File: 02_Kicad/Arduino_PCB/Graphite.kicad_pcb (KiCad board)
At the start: 2 copper layers, 68.6 x 53.3 mm, 21 parts, among them J1 Power, J2 Digital/PWM, J3 Analog, J4 Digital/PWM, U1 LTC1050, U2 HC05

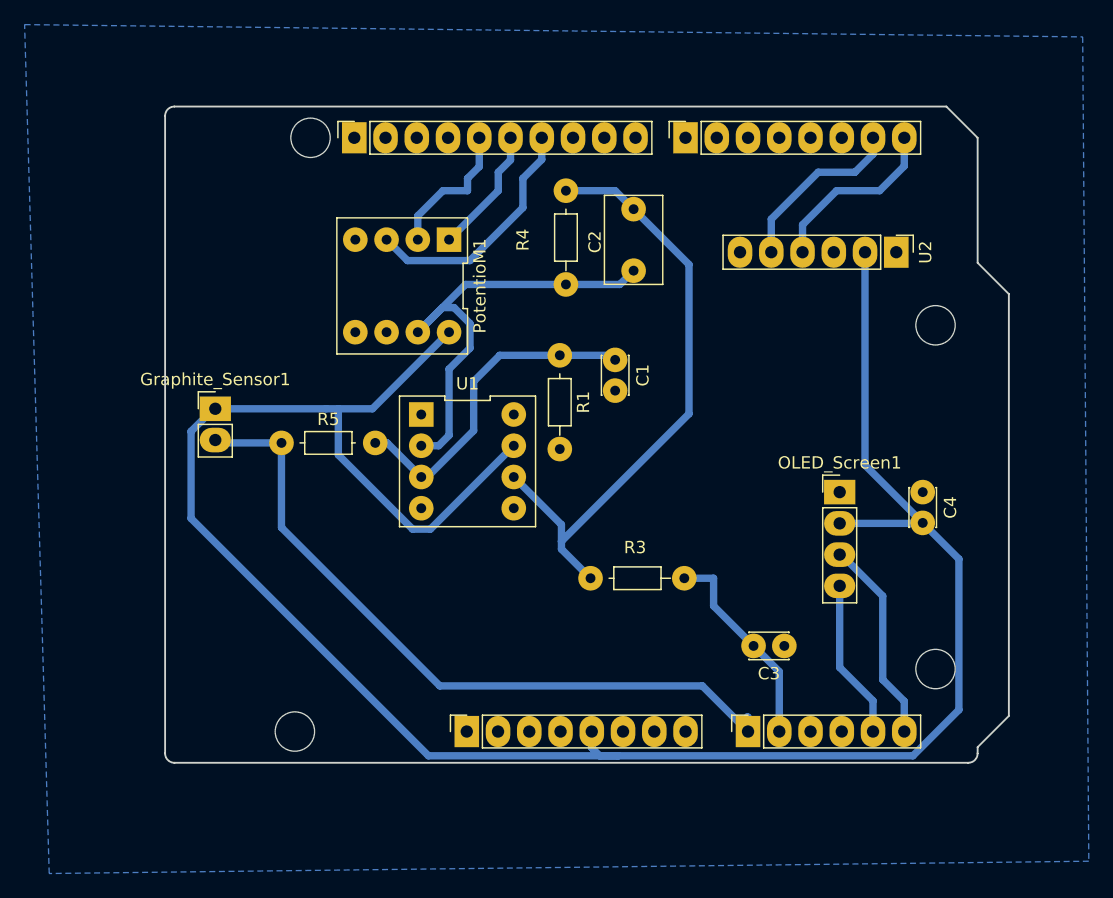
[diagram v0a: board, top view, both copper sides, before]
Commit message: Rectification Kicad
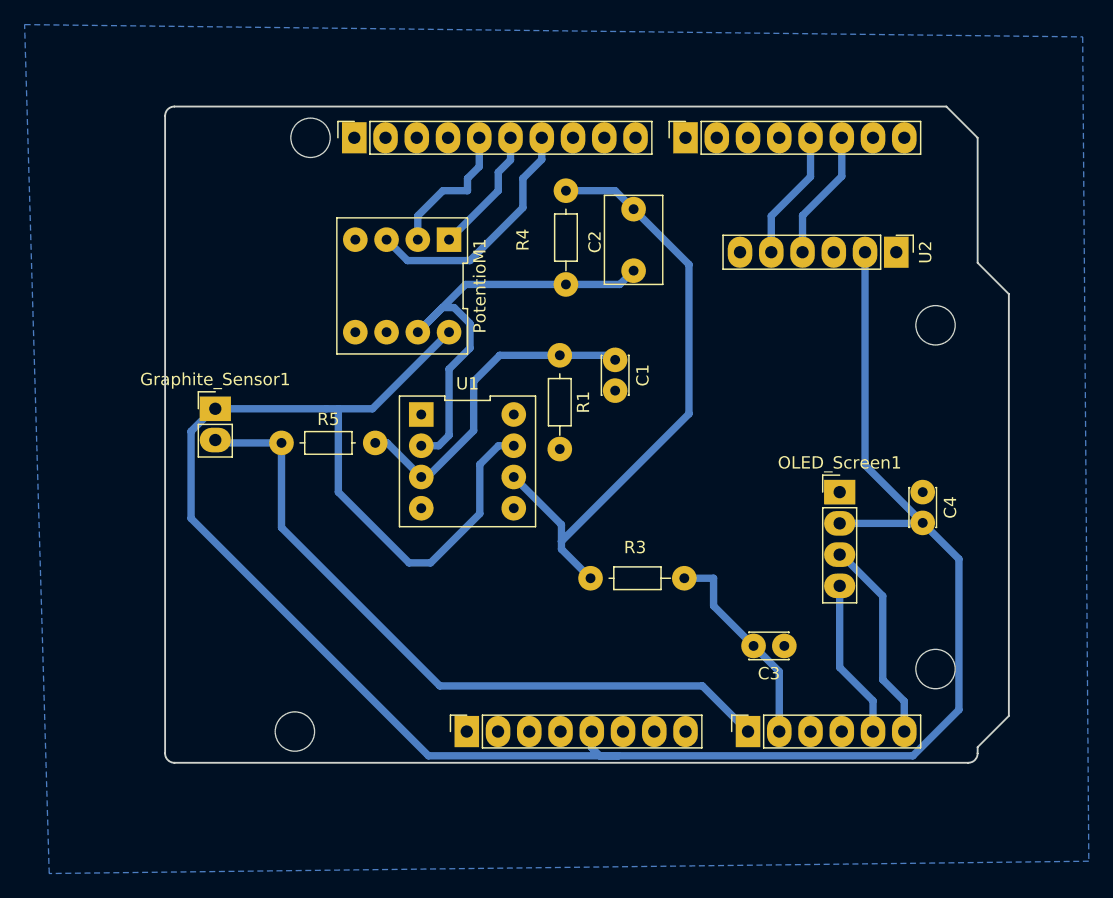
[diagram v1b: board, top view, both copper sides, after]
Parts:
- R3: value 100k -> 1K
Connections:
- J4 pad 5: /*3 -> BluetoothInput
- J4 pad 6: /2 -> BluetoothOutput
- J4 pad 7: BluetoothInput -> /TX/1
- J4 pad 8: BluetoothOutput -> /RX/0
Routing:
- net +5V: track 177.5 -> 183.9 mm
- net BluetoothOutput: track 14.8 -> 10.6 mm
- net BluetoothInput: track 14.5 -> 10.6 mm
- net Flex_Out: track 58.4 -> 57.1 mm
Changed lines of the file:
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@@
 	(net 18 "SDA")
 	(net 19 "/4")
-	(net 20 "/2")
+	(net 20 "/TX{slash}1")
 	(net 21 "/*6")
 	(net 22 "/*5")
 	(net 23 "D12")
-	(net 24 "/*3")
+	(net 24 "/RX{slash}0")
 	(net 25 "+3V3")
 	(net 26 "VCC")
@@
 			(layers "*.Cu" "*.Mask")
 			(remove_unused_layers no)
-			(net 24 "/*3")
+			(net 10 "BluetoothInput")
 			(pinfunction "Pin_5")
-			(pintype "passive+no_connect")
+			(pintype "passive")
 		)
 		(pad "6" thru_hole oval
@@
 			(layers "*.Cu" "*.Mask")
 			(remove_unused_layers no)
-			(net 20 "/2")
+			(net 17 "BluetoothOutput")
 			(pinfunction "Pin_6")
-			(pintype "passive+no_connect")
+			(pintype "passive")
 		)
 		(pad "7" thru_hole oval
@@
 			(layers "*.Cu" "*.Mask")
 			(remove_unused_layers no)
-			(net 10 "BluetoothInput")
+			(net 20 "/TX{slash}1")
 			(pinfunction "Pin_7")
-			(pintype "passive")
+			(pintype "passive+no_connect")
 		)
 		(pad "8" thru_hole oval
@@
 			(layers "*.Cu" "*.Mask")
 			(remove_unused_layers no)
-			(net 17 "BluetoothOutput")
+			(net 24 "/RX{slash}0")
 			(pinfunction "Pin_8")
-			(pintype "passive")
+			(pintype "passive+no_connect")
 		)
 		(embedded_fonts no)
@@
 			)
 		)
-		(property "Value" "100k"
+		(property "Value" "1K"
 			(at 3.81 1.92 0)
 			(layer "F.Fab")
@@
 	)
 	(segment
+		(start 129 79.75)
+		(end 129 75.75)
+		(width 0.6)
+		(layer "B.Cu")
+		(net 3)
+	)
+	(segment
 		(start 120.275 71.225)
 		(end 126.5 65)
@@
 	)
 	(segment
+		(start 129 75.75)
+		(end 130.52 74.23)
+		(width 0.6)
+		(layer "B.Cu")
+		(net 3)
+	)
+	(segment
 		(start 138.741 99.431)
 		(end 140.25 99.431)
@@
 	)
 	(segment
+		(start 117.5 78)
+		(end 123.25 83.75)
+		(width 0.6)
+		(layer "B.Cu")
+		(net 3)
+	)
+	(segment
+		(start 125 83.75)
+		(end 129 79.75)
+		(width 0.6)
+		(layer "B.Cu")
+		(net 3)
+	)
+	(segment
+		(start 123.25 83.75)
+		(end 125 83.75)
+		(width 0.6)
+		(layer "B.Cu")
+		(net 3)
+	)
+	(segment
 		(start 160.31 75.81)
 		(end 165 80.5)
@@
 	)
 	(segment
-		(start 117.5 71.225)
-		(end 120.275 71.225)
+		(start 130.52 74.23)
+		(end 131.76 74.23)
 		(width 0.6)
 		(layer "B.Cu")
@@
 	)
 	(segment
-		(start 138.1 97.46)
-		(end 138.1 98.79)
+		(start 117.5 71.225)
+		(end 120.275 71.225)
 		(width 0.6)
 		(layer "B.Cu")
@@
 	)
 	(segment
-		(start 117.5 74.975578)
-		(end 117.5 71.225)
+		(start 138.1 97.46)
+		(end 138.1 98.79)
 		(width 0.6)
 		(layer "B.Cu")
@@
 	)
 	(segment
-		(start 124.979 81.011)
-		(end 123.535422 81.011)
-		(width 0.6)
-		(layer "B.Cu")
-		(net 3)
-	)
-	(segment
 		(start 105.529 73.060423)
 		(end 105.529 80.136628)
@@
 	)
 	(segment
-		(start 123.535422 81.011)
-		(end 117.5 74.975578)
-		(width 0.6)
-		(layer "B.Cu")
-		(net 3)
-	)
-	(segment
 		(start 164.96 80.54)
 		(end 165 80.5)
@@
 	)
 	(segment
-		(start 167.941 95.694577)
-		(end 167.941 83.441)
+		(start 117.5 71.225)
+		(end 117.5 78)
 		(width 0.6)
 		(layer "B.Cu")
@@
 	)
 	(segment
-		(start 131.76 74.23)
-		(end 124.979 81.011)
+		(start 167.941 95.694577)
+		(end 167.941 83.441)
 		(width 0.6)
 		(layer "B.Cu")
@@
 	)
 	(segment
-		(start 147.09 93.75)
-		(end 150.8 97.46)
-		(width 0.6)
-		(layer "B.Cu")
-		(net 9)
-	)
-	(segment
 		(start 112.88 74)
 		(end 107.735 74)
@@
 	)
 	(segment
-		(start 150.8 97.46)
-		(end 150.8 96.3)
-		(width 0.6)
-		(layer "B.Cu")
-		(net 9)
-	)
-	(segment
 		(start 112.88 80.88)
 		(end 125.75 93.75)
@@
 	)
 	(segment
-		(start 150.8 96.3)
-		(end 150.75 96.25)
+		(start 147.09 93.75)
+		(end 150.8 97.46)
 		(width 0.6)
 		(layer "B.Cu")
@@
 	)
 	(segment
-		(start 159.49 52)
-		(end 160.96 50.53)
-		(width 0.6)
-		(layer "B.Cu")
-		(net 10)
-	)
-	(segment
-		(start 160.96 50.53)
-		(end 160.96 49.2)
-		(width 0.6)
-		(layer "B.Cu")
-		(net 10)
-	)
-	(segment
-		(start 156.5 52)
-		(end 159.49 52)
+		(start 152.69 55.56)
+		(end 155.88 52.37)
 		(width 0.6)
 		(layer "B.Cu")
@@
 	(segment
 		(start 152.69 58.5)
-		(end 152.69 55.81)
+		(end 152.69 55.56)
 		(width 0.6)
 		(layer "B.Cu")
@@
 	)
 	(segment
-		(start 152.69 55.81)
-		(end 156.5 52)
+		(start 155.88 52.37)
+		(end 155.88 49.2)
 		(width 0.6)
 		(layer "B.Cu")
@@
 	)
 	(segment
-		(start 161.5 53.5)
-		(end 163.5 51.5)
+		(start 158.42 52.33)
+		(end 158.42 49.2)
 		(width 0.6)
 		(layer "B.Cu")
@@
 	)
 	(segment
-		(start 155.23 56.27)
-		(end 158 53.5)
-		(width 0.6)
-		(layer "B.Cu")
-		(net 17)
-	)
-	(segment
-		(start 158 53.5)
-		(end 161.5 53.5)
-		(width 0.6)
-		(layer "B.Cu")
-		(net 17)
-	)
-	(segment
-		(start 163.5 51.5)
-		(end 163.5 49.2)
+		(start 155.23 58.5)
+		(end 155.23 55.52)
 		(width 0.6)
 		(layer "B.Cu")
@@
 	)
 	(segment
-		(start 155.23 58.5)
-		(end 155.23 56.27)
+		(start 155.23 55.52)
+		(end 158.42 52.33)
 		(width 0.6)
 		(layer "B.Cu")
